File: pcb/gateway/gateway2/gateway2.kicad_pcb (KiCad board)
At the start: 4 copper layers, 77 x 47 mm, 104 parts, among them J1 Conn_ARM_JTAG_SWD_10, J2 RJ45_Kycon_G7LX-A88S7-BP-GY, J8 Conn_01x07, P1 USB_C_Plug_USB2.0, SW1 RST, SW2 BOOT, U1 RP2354B, U2 W6300-Q, U3 RT6150AGQW, U8 74AHC125, Y1 ABM8-272-T3, Y2 25MHz

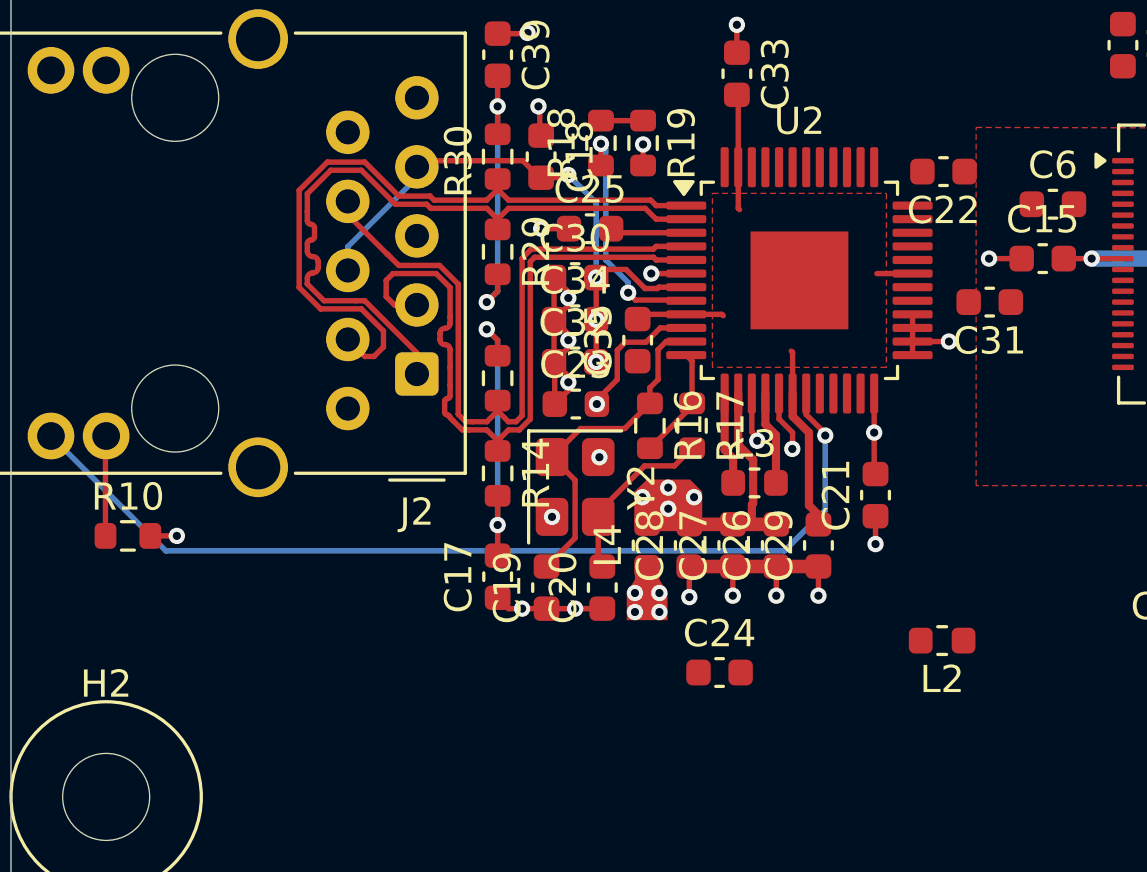
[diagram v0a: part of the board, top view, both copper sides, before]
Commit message: Wiznet power routing is mostly done.
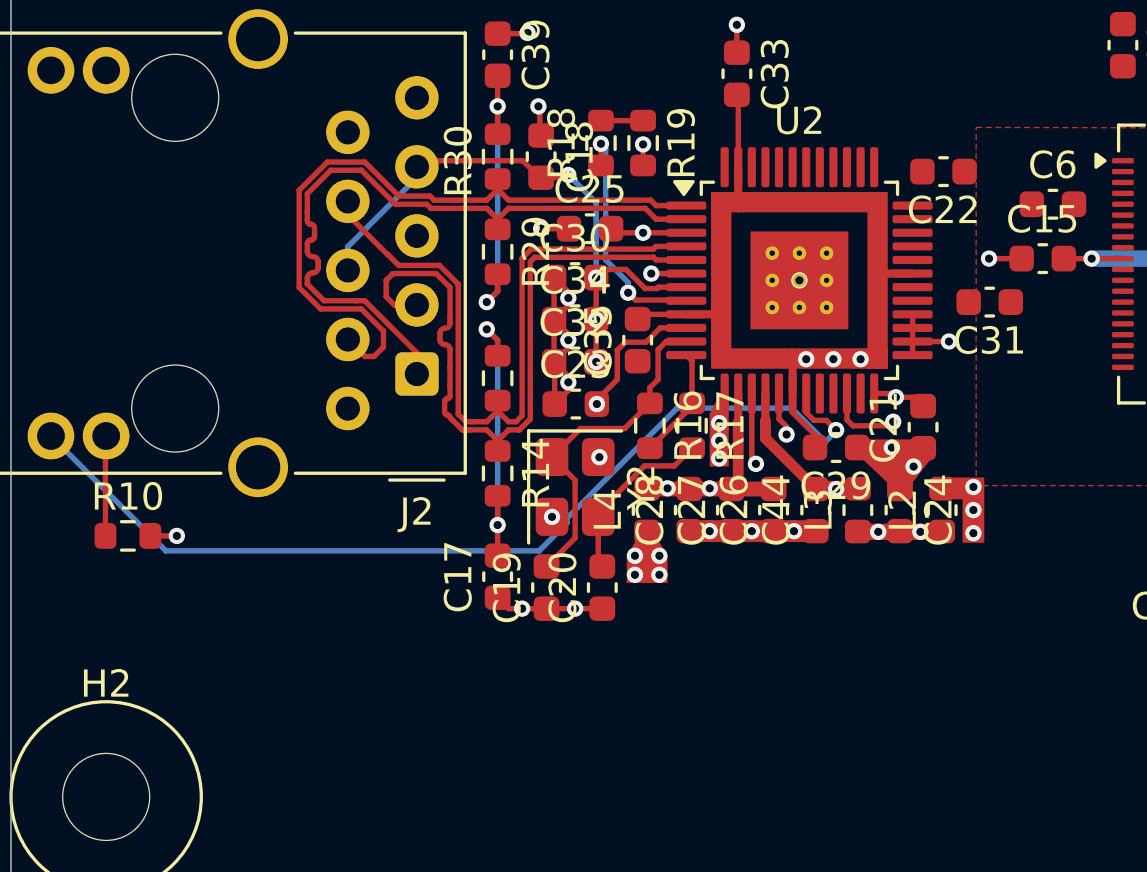
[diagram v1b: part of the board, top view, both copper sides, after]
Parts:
- added C44: 100n, Capacitor_SMD:C_0603_1608Metric, F.Cu at (126.1, 89.5)
- U2: footprint Package_QFP:LQFP-48-1EP_7x7mm_P0.5mm_EP3.6x3.6mm -> Package_QFP:LQFP-48-1EP_7x7mm_P0.5mm_EP3.6x3.6mm_ThermalVias
- moved C24 8.93 mm to (129.2, 89.5), turned to -90 degrees
- moved L2 4.80 mm to (130.8, 89.5), turned to 90 degrees
- moved L3 3.93 mm to (127.7, 89.5), turned to 90 degrees
- moved C29 3.66 mm to (126.8, 87.2), turned to 180 degrees
- moved C21 3.05 mm to (130.1, 86.4)
- moved C26 1.30 mm to (124.5, 89.5)
- moved C27 1.30 mm to (123.0, 89.5)
- moved C28 1.30 mm to (121.5, 89.5)
- moved L4 1.30 mm to (119.9, 89.5)
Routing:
- net 1V2A: track 6.27 -> 21.8 mm, vias 0 -> 2
- net 1V2D: track 15.6 -> 24.8 mm, vias 0 -> 6
- net GND: track 67.6 -> 59.4 mm, vias 61 -> 62
- net Net-(U2-1V2O): track 3.42 -> 9.82 mm, vias 0 -> 5
- net 3V3A: track 41.3 -> 36.0 mm, vias 8 -> 6
- net Net-(J2-LEDG_K): track 0.00 -> 2.82 mm, vias 0 -> 1
- net +3V3: track 32.3 -> 31.2 mm
- removed copper zone on F.Cu, net 1V2D

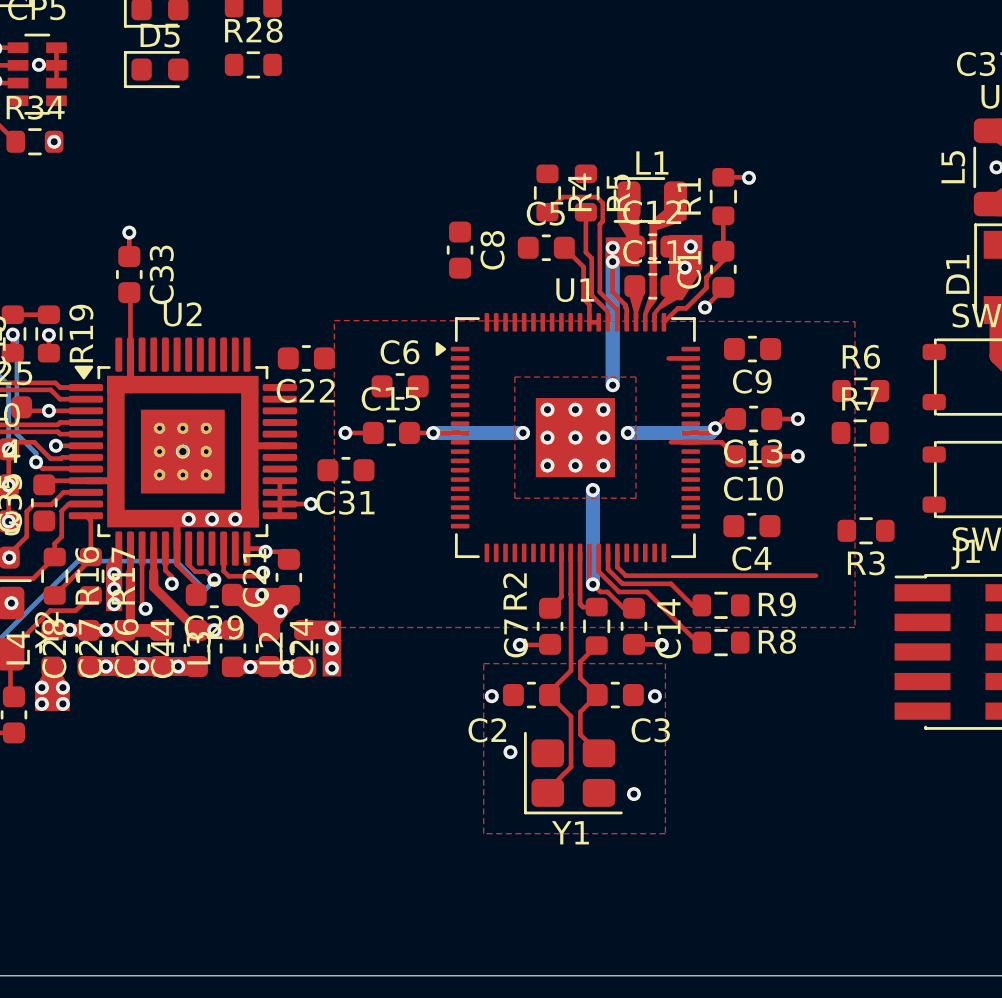
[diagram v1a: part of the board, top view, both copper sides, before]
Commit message: Cross-routing Wiznet SPI.
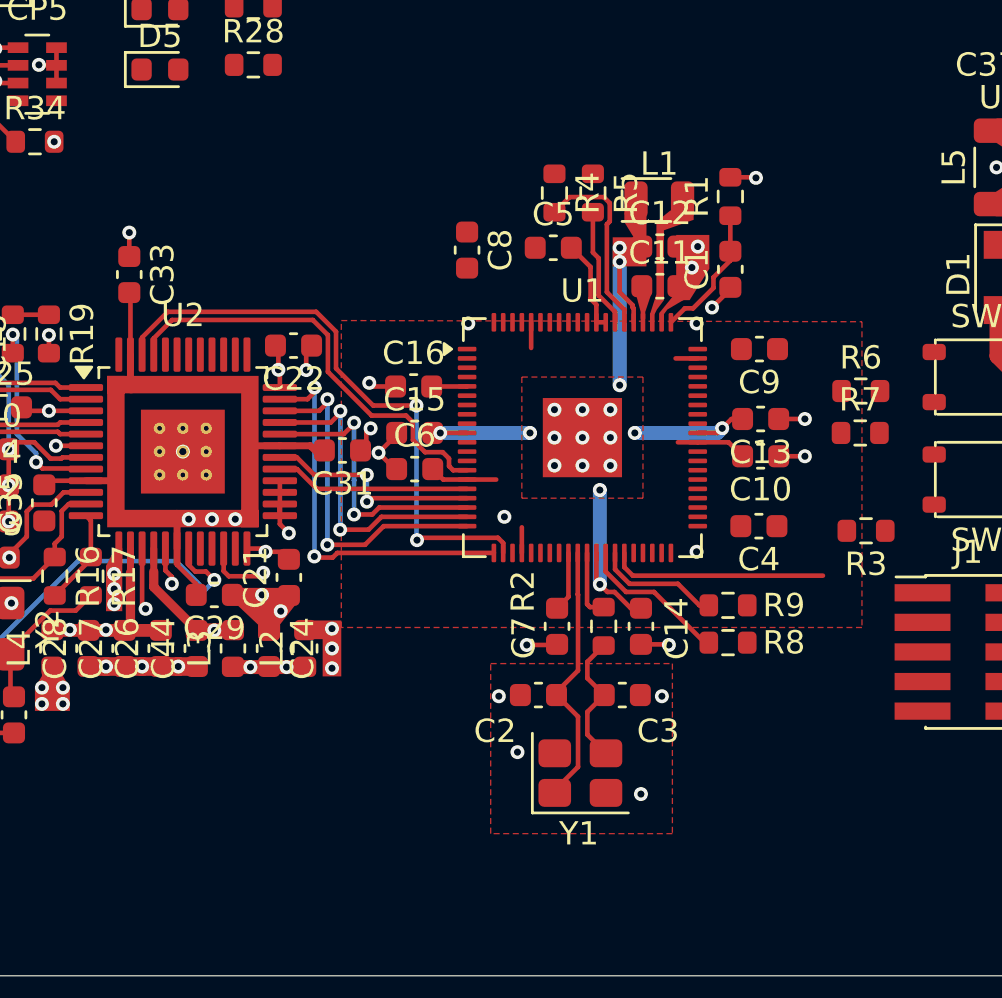
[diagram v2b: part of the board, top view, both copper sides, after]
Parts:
- added C16: 100n, Capacitor_SMD:C_0603_1608Metric, F.Cu at (135.4, 78.2)
- moved C6 3.60 mm to (135.4, 81.8)
- moved C15 1.00 mm to (135.4, 80.2)
- moved C31 0.86 mm to (132.3, 81.0)
- moved C22 0.78 mm to (130.2, 76.5)
- moved C1 0.30 mm to (149.0, 73.2)
- moved C10 0.30 mm to (150.3, 81.2)
- moved C13 0.30 mm to (150.3, 79.6)
- moved C3 0.30 mm to (144.4, 91.5)
- moved C5 0.30 mm to (141.4, 72.2)
- moved C7 0.30 mm to (141.6, 88.5)
- moved C9 0.30 mm to (150.2, 76.6)
- moved R1 0.30 mm to (149.0, 70.0)
- moved R2 0.30 mm to (143.6, 88.5)
- moved R8 0.30 mm to (148.9, 89.2)
- moved R9 0.30 mm to (148.9, 87.6)
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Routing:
- net /WizNet/RST: track 0.00 -> 25.6 mm, vias 0 -> 2
- net /WizNet/INT: track 0.00 -> 18.7 mm
- net /WizNet/QSPI_Q3: track 0.00 -> 16.7 mm, vias 0 -> 2
- net /WizNet/QSPI_Q2: track 0.00 -> 14.7 mm, vias 0 -> 2
- net /WizNet/QSPI_Q1: track 0.00 -> 13.6 mm, vias 0 -> 2
- net /WizNet/QSPI_Q0: track 0.00 -> 12.3 mm, vias 0 -> 2
- net /WizNet/QSPI_CLK: track 0.00 -> 9.56 mm, vias 0 -> 2
- net +3V3: track 31.2 -> 39.7 mm, vias 16 -> 21
- net /WizNet/QSPI_CS: track 0.00 -> 8.39 mm
- net GND: track 59.4 -> 64.2 mm, vias 62 -> 65
- net 1V2D: track 24.8 -> 26.9 mm

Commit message: Routing some more.
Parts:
- removed D2: PMEG6010ELRX, Diode_SMD:Nexperia_CFP3_SOD-123W
- U2: footprint Package_QFP:LQFP-48-1EP_7x7mm_P0.5mm_EP3.6x3.6mm_ThermalVias -> Package_QFP:LQFP-48-1EP_7x7mm_P0.5mm_EP3.6x3.6mm
- moved D3 39.4 mm to (131.3, 98.2)
- moved R26 39.3 mm to (134.3, 98.2)
- moved D4 38.3 mm to (131.3, 99.8)
- moved R27 38.3 mm to (134.3, 99.8)
- moved R28 37.4 mm to (134.3, 101.3)
- moved D5 37.3 mm to (131.3, 101.3)
- moved J1 9.53 mm to (160.0, 99.1), turned to 90 degrees
- moved R3 4.85 mm to (150.2, 86.0)
- moved R7 4.04 mm to (152.7, 76.7), turned to 90 degrees
- moved R6 3.91 mm to (151.1, 76.7), turned to 90 degrees
- moved C8 1.60 mm to (139.1, 71.5)
- moved R11 0.91 mm to (100.8, 69.6)
- moved C9 0.70 mm to (149.6, 76.7), turned to -90 degrees
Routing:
- net POWER_SAVE: track 7.09 -> 55.0 mm, vias 2 -> 3
- net Net-(J2-LEDG_K): track 2.82 -> 46.7 mm
- net /USB_D-: track 1.98 -> 36.9 mm, vias 0 -> 1
- net /USB_D+: track 1.70 -> 35.4 mm, vias 0 -> 1
- net Net-(J1-~{RESET}): track 0.00 -> 29.7 mm
- net VBUS_MONITOR: track 2.31 -> 29.8 mm, vias 0 -> 2
- net GND: track 64.2 -> 80.0 mm, vias 65 -> 74
- net Net-(U1-~{QSPI_SS}): track 0.00 -> 14.4 mm, vias 0 -> 2
- net Net-(J1-SWDIO/TMS): track 0.00 -> 13.8 mm
- net Net-(J1-SWCLK/TCK): track 0.00 -> 12.8 mm
- net Net-(R7-Pad1): track 0.00 -> 10.2 mm
- net +3V3: track 39.7 -> 46.7 mm, vias 21 -> 23
- net Net-(J2-LEDG_A): track 0.00 -> 3.69 mm
- net Net-(U1-RUN): track 9.29 -> 5.72 mm
- net Net-(J2-LEDY_K): track 35.7 -> 38.5 mm

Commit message: Compactifying bricklet connection.
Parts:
- R4: value 27? -> 27
- R5: value 85? -> 27
- moved R35 8.43 mm to (118.5, 67.5), turned to 0 degrees
- moved C42 2.80 mm to (106.7, 66.7), turned to -90 degrees
- moved JP10 1.06 mm to (111.8, 67.4)
- moved JP9 1.03 mm to (115.1, 67.4)
- moved R34 0.65 mm to (118.5, 67.5)
- moved CP5 0.50 mm to (118.8, 64.8)
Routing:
- net /CS_2: track 19.6 -> 32.5 mm, vias 3 -> 4
- net /MOSI: track 0.82 -> 11.8 mm, vias 1 -> 2
- net /CS_1: track 0.00 -> 10.6 mm
- net /MISO: track 1.14 -> 4.28 mm
- net +3V3: track 46.7 -> 44.4 mm, vias 23 -> 22
- net GND: track 80.0 -> 78.6 mm, vias 74 -> 75
- net /CLK: track 1.18 -> 2.35 mm
- net Net-(JP10-B): track 2.57 -> 2.00 mm
- net Net-(J8-Pin_6): track 6.46 -> 5.96 mm
- net +5V: vias 0 -> 1

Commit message: Trying to fit 6 bricklet connectors.
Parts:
- added C45: 100n, Capacitor_SMD:C_0603_1608Metric, F.Cu at (120.8, 66.7)
- added C46: 100n, Capacitor_SMD:C_0603_1608Metric, F.Cu at (135.8, 66.7)
- added C47: 100n, Capacitor_SMD:C_0603_1608Metric, F.Cu at (118.2, 93.0)
- added C48: 100n, Capacitor_SMD:C_0603_1608Metric, F.Cu at (133.2, 93.0)
- added C49: 100n, Capacitor_SMD:C_0603_1608Metric, F.Cu at (133.1, 134.3)
- added CP10: C_Array_4x0612, AVX_Capacitor_Array:C_Array_4x0612, F.Cu at (145.2, 132.4)
- added CP6: C_Array_4x0612, AVX_Capacitor_Array:C_Array_4x0612, F.Cu at (132.9, 64.8)
- added CP7: C_Array_4x0612, AVX_Capacitor_Array:C_Array_4x0612, F.Cu at (147.9, 64.8)
- added CP8: C_Array_4x0612, AVX_Capacitor_Array:C_Array_4x0612, F.Cu at (106.1, 94.9)
- added CP9: C_Array_4x0612, AVX_Capacitor_Array:C_Array_4x0612, F.Cu at (121.2, 94.9)
- added J10: Conn_01x07, Connector_JST:JST_GH_BM07B-GHS-TBT_1x07-1MP_P1.25mm_Vertical, F.Cu at (142.0, 60.0)
- added J11: Conn_01x07, Connector_JST:JST_GH_BM07B-GHS-TBT_1x07-1MP_P1.25mm_Vertical, F.Cu at (112.0, 99.7)
- added J12: Conn_01x07, Connector_JST:JST_GH_BM07B-GHS-TBT_1x07-1MP_P1.25mm_Vertical, F.Cu at (127.0, 99.7)
- added J13: Conn_01x07, Connector_JST:JST_GH_BM07B-GHS-TBT_1x07-1MP_P1.25mm_Vertical, F.Cu at (139.3, 127.7)
- added J9: Conn_01x07, Connector_JST:JST_GH_BM07B-GHS-TBT_1x07-1MP_P1.25mm_Vertical, F.Cu at (127.0, 60.0)
- added JP11: SolderJumper_2_Open, Jumper:SolderJumper-2_P1.3mm_Open_RoundedPad1.0x1.5mm, B.Cu at (129.2, 67.4)
- added JP12: SolderJumper_2_Bridged, Jumper:SolderJumper-2_P1.3mm_Bridged_RoundedPad1.0x1.5mm, B.Cu at (125.9, 67.4)
- added JP13: SolderJumper_2_Open, Jumper:SolderJumper-2_P1.3mm_Open_RoundedPad1.0x1.5mm, B.Cu at (144.2, 67.4)
- added JP14: SolderJumper_2_Bridged, Jumper:SolderJumper-2_P1.3mm_Bridged_RoundedPad1.0x1.5mm, B.Cu at (140.9, 67.4)
- added JP15: SolderJumper_2_Open, Jumper:SolderJumper-2_P1.3mm_Open_RoundedPad1.0x1.5mm, B.Cu at (109.8, 92.3)
- added JP16: SolderJumper_2_Bridged, Jumper:SolderJumper-2_P1.3mm_Bridged_RoundedPad1.0x1.5mm, B.Cu at (113.1, 92.3)
- added JP17: SolderJumper_2_Open, Jumper:SolderJumper-2_P1.3mm_Open_RoundedPad1.0x1.5mm, B.Cu at (124.8, 92.3)
- added JP18: SolderJumper_2_Bridged, Jumper:SolderJumper-2_P1.3mm_Bridged_RoundedPad1.0x1.5mm, B.Cu at (128.2, 92.3)
- added JP19: SolderJumper_2_Open, Jumper:SolderJumper-2_P1.3mm_Open_RoundedPad1.0x1.5mm, B.Cu at (141.5, 135.1)
- added JP20: SolderJumper_2_Bridged, Jumper:SolderJumper-2_P1.3mm_Bridged_RoundedPad1.0x1.5mm, B.Cu at (138.2, 135.1)
- added R36: 100k, Resistor_SMD:R_0603_1608Metric, F.Cu at (132.7, 67.5)
- added R37: 10k, Resistor_SMD:R_0603_1608Metric, B.Cu at (132.7, 67.5)
- added R39: 100k, Resistor_SMD:R_0603_1608Metric, F.Cu at (147.7, 67.5)
- added R40: 10k, Resistor_SMD:R_0603_1608Metric, B.Cu at (147.7, 67.5)
- added R42: 100k, Resistor_SMD:R_0603_1608Metric, F.Cu at (106.3, 92.2)
- added R43: 10k, Resistor_SMD:R_0603_1608Metric, B.Cu at (106.3, 92.2)
- added R44: 100k, Resistor_SMD:R_0603_1608Metric, F.Cu at (121.3, 92.2)
- added R45: 10k, Resistor_SMD:R_0603_1608Metric, B.Cu at (121.3, 92.2)
- added R46: 100k, Resistor_SMD:R_0603_1608Metric, F.Cu at (145.0, 135.1)
- added R47: 10k, Resistor_SMD:R_0603_1608Metric, B.Cu at (145.0, 135.1)
- added RN10: R_Pack04, Resistor_SMD:R_Array_Concave_4x0603, F.Cu at (140.6, 133.4)
- added RN6: R_Pack04, Resistor_SMD:R_Array_Concave_4x0603, F.Cu at (128.3, 65.8)
- added RN7: R_Pack04, Resistor_SMD:R_Array_Concave_4x0603, F.Cu at (143.3, 65.8)
- added RN8: R_Pack04, Resistor_SMD:R_Array_Concave_4x0603, F.Cu at (110.7, 93.9)
- added RN9: R_Pack04, Resistor_SMD:R_Array_Concave_4x0603, F.Cu at (125.8, 93.9)
- added U10: 74AHC125, Package_DFN_QFN:DHVQFN-14-1EP_2.5x3mm_P0.5mm_EP1x1.5mm, F.Cu at (139.2, 65.6)
- added U11: 74AHC125, Package_DFN_QFN:DHVQFN-14-1EP_2.5x3mm_P0.5mm_EP1x1.5mm, F.Cu at (114.8, 94.1)
- added U12: 74AHC125, Package_DFN_QFN:DHVQFN-14-1EP_2.5x3mm_P0.5mm_EP1x1.5mm, F.Cu at (129.9, 94.1)
- added U13: 74AHC125, Package_DFN_QFN:DHVQFN-14-1EP_2.5x3mm_P0.5mm_EP1x1.5mm, F.Cu at (136.4, 133.3)
- added U9: 74AHC125, Package_DFN_QFN:DHVQFN-14-1EP_2.5x3mm_P0.5mm_EP1x1.5mm, F.Cu at (124.2, 65.6)
- moved D3 49.2 mm to (134.6, 49.1)
- moved D4 49.2 mm to (134.6, 50.6)
- moved R26 49.2 mm to (137.6, 49.1)
- moved R27 49.2 mm to (137.6, 50.6)
- moved D5 49.2 mm to (134.6, 52.2)
- moved R28 49.2 mm to (137.6, 52.2)
- moved C17 4.07 mm to (113.7, 87.9), turned to 0 degrees
- moved C18 2.50 mm to (116.0, 74.0)
- moved C19 2.50 mm to (116.2, 89.8)
- moved C20 2.50 mm to (118.2, 89.8)
- moved C21 2.50 mm to (130.1, 83.9)
- moved C22 2.50 mm to (130.2, 74.0)
- moved C23 2.50 mm to (117.3, 83.0)
- moved C24 2.50 mm to (129.2, 87.0)
- moved C25 2.50 mm to (117.8, 76.6)
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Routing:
- net /MOSI: track 11.8 -> 70.7 mm, vias 2 -> 12
- net /CS_6: track 0.00 -> 30.5 mm, vias 0 -> 4
- net /CS_4: track 0.00 -> 30.5 mm, vias 0 -> 4
- net /CS_3: track 0.00 -> 30.5 mm, vias 0 -> 4
- net /CS_5: track 0.00 -> 30.5 mm, vias 0 -> 4
- net GND: track 78.6 -> 108.0 mm, vias 75 -> 106
- net /MISO: track 4.28 -> 25.7 mm, vias 1 -> 6
- net /CS_1: track 10.6 -> 30.5 mm, vias 0 -> 4
- net +3V3: track 44.4 -> 61.9 mm, vias 22 -> 32
- net Net-(RN10-R1.2): track 0.00 -> 12.5 mm, vias 0 -> 2
- net Net-(RN9-R1.2): track 0.00 -> 12.5 mm, vias 0 -> 2
- net Net-(RN8-R1.2): track 0.00 -> 12.5 mm, vias 0 -> 2
- net Net-(RN6-R1.2): track 0.00 -> 12.5 mm, vias 0 -> 2
- net Net-(RN7-R1.2): track 0.00 -> 12.5 mm, vias 0 -> 2
- net /CLK: track 2.35 -> 14.1 mm, vias 1 -> 6
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
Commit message: All stuff is on board.
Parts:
- moved C49 43.9 mm to (148.2, 93.1), turned to 90 degrees
- moved R46 43.6 mm to (136.3, 92.3), turned to 180 degrees
- moved R47 43.6 mm to (136.3, 92.3), turned to 180 degrees
- moved JP20 42.9 mm to (143.1, 92.4), turned to 0 degrees
- moved JP19 42.7 mm to (139.8, 92.4), turned to 0 degrees
- moved U13 40.0 mm to (144.8, 94.2), turned to 0 degrees
- moved RN10 39.5 mm to (140.7, 94.0), turned to 90 degrees
- moved CP10 38.5 mm to (136.1, 95.0), turned to 180 degrees
- moved J13 28.0 mm to (142.0, 99.8), turned to 180 degrees
- moved Y1 10.4 mm to (134.5, 88.2), turned to -90 degrees
- moved C3 6.83 mm to (137.8, 89.5)
- moved C2 5.47 mm to (137.8, 86.8), turned to 180 degrees
- moved C17 1.06 mm to (114.4, 88.7), turned to 90 degrees
- moved C7 0.95 mm to (141.6, 87.5)
- moved JP15 0.10 mm to (109.8, 92.4)
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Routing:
- net GND: track 108.0 -> 104.0 mm
- net Net-(C3-Pad2): track 5.68 -> 9.24 mm
- net Net-(U1-XIN): track 11.3 -> 14.1 mm
- net /WizNet/RST: track 25.6 -> 27.9 mm
- net 3V3A: track 36.0 -> 38.3 mm, vias 6 -> 8
- net /WizNet/INT: track 18.7 -> 20.8 mm
- net /WizNet/QSPI_CS: track 8.39 -> 10.5 mm
- net /CS_2: track 32.5 -> 30.5 mm
- net /WizNet/QSPI_CLK: track 9.56 -> 11.3 mm
- net /WizNet/QSPI_Q0: track 12.3 -> 13.7 mm
- net Net-(J2-LEDY_K): track 38.5 -> 37.2 mm
- net Net-(J2-LEDG_K): track 46.7 -> 45.4 mm
- net +3V3: track 61.9 -> 60.6 mm
- net /WizNet/QSPI_Q3: track 16.7 -> 17.6 mm
- net /WizNet/QSPI_Q1: track 13.6 -> 14.3 mm
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- removed copper zone on F.Cu, net GND

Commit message: Still routing.
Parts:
- moved C14 0.54 mm to (144.8, 88.8)
- moved R2 0.50 mm to (143.2, 88.8)
- moved C4 0.33 mm to (150.6, 84.2)
- moved R3 0.33 mm to (150.6, 86.0)
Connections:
- U1 pad 38: unconnected-(U1-GPIO30-Pad38) -> /CS_4
- U1 pad 39: unconnected-(U1-GPIO31-Pad39) -> /CS_5
- U1 pad 40: unconnected-(U1-GPIO32-Pad40) -> /CS_6
- U1 pad 42: /CS_3 -> /CS_2
- U1 pad 43: /CS_2 -> /CS_1
- U1 pad 44: /CS_1 -> /CS_3
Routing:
- net /CLK: track 14.1 -> 177.8 mm, vias 6 -> 12
- net /MISO: track 25.7 -> 180.3 mm, vias 6 -> 13
- net /MOSI: track 70.7 -> 213.5 mm, vias 12 -> 13
- net +5V: track 4.60 -> 137.2 mm, vias 6 -> 12
- net /CS_4: track 30.5 -> 67.4 mm, vias 4 -> 5
- net /CS_5: track 30.5 -> 52.7 mm, vias 4 -> 5
- net Net-(U1-~{QSPI_SS}): track 5.09 -> 24.0 mm
- net /CS_6: track 30.5 -> 38.2 mm, vias 4 -> 5
- net POWER_SAVE: track 54.5 -> 60.8 mm
- net VBUS_MONITOR: track 29.8 -> 35.8 mm
- net /CS_1: track 30.5 -> 28.5 mm
- net /CS_2: track 30.5 -> 28.5 mm
- net /CS_3: track 30.5 -> 32.2 mm, vias 4 -> 5
- net Net-(U1-RUN): track 5.72 -> 7.07 mm
- net Net-(J2-LEDY_K): track 37.2 -> 37.4 mm, vias 1 -> 3
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
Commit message: Walking through DRC.
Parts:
- D4: value SERVER GOOD -> SRV GOOD
- moved C38 69.0 mm to (105.6, 69.6), turned to 180 degrees
- moved R26 26.1 mm to (125.2, 72.0)
- moved D3 23.8 mm to (128.2, 72.0), turned to 180 degrees
- moved R27 23.3 mm to (125.2, 70.5)
- moved D4 20.8 mm to (128.2, 70.5), turned to 180 degrees
- moved R28 20.7 mm to (125.2, 68.8)
- moved D5 17.8 mm to (128.2, 68.8), turned to 180 degrees
- moved C33 1.97 mm to (122.0, 72.5), turned to 0 degrees
- moved C10 1.55 mm to (151.8, 81.2)
- moved C13 1.55 mm to (151.8, 79.6)
- moved C4 1.32 mm to (151.8, 84.5)
- moved R3 1.30 mm to (151.8, 86.0)
- moved C22 0.05 mm to (130.2, 74.0)
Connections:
- R26 pad 1: Net-(U1-GPIO0) -> Net-(U1-GPIO2)
- R27 pad 1: Net-(U1-GPIO2) -> Net-(U1-GPIO1)
- R28 pad 1: Net-(U1-GPIO1) -> Net-(U1-GPIO0)
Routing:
- net /CS_2: track 28.5 -> 85.6 mm, vias 4 -> 5
- net /CS_1: track 28.5 -> 67.7 mm, vias 4 -> 5
- net /CS_3: track 32.2 -> 65.7 mm
- net Net-(U1-GPIO0): track 0.00 -> 20.3 mm
- net Net-(U1-GPIO1): track 0.00 -> 18.3 mm
- net Net-(U1-GPIO2): track 0.00 -> 17.2 mm
- net GNDPWR: track 19.9 -> 35.9 mm
- net +3V3: track 60.6 -> 76.2 mm, vias 38 -> 39
- net GND: track 103.8 -> 107.3 mm, vias 106 -> 113
- net +1V1: track 28.8 -> 31.6 mm
- net Net-(U1-RUN): track 7.07 -> 8.58 mm
- net Net-(D5-A): track 0.00 -> 1.41 mm
- net Net-(D4-A): track 0.00 -> 1.41 mm
- net Net-(D3-A): track 0.00 -> 1.41 mm
- net /CLK: track 177.8 -> 176.5 mm, vias 12 -> 7
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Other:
- board size 77 x 47 mm -> 77.2 x 47.2 mm
